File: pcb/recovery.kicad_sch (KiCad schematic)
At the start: 9 parts, among them Q1 SiS454DN

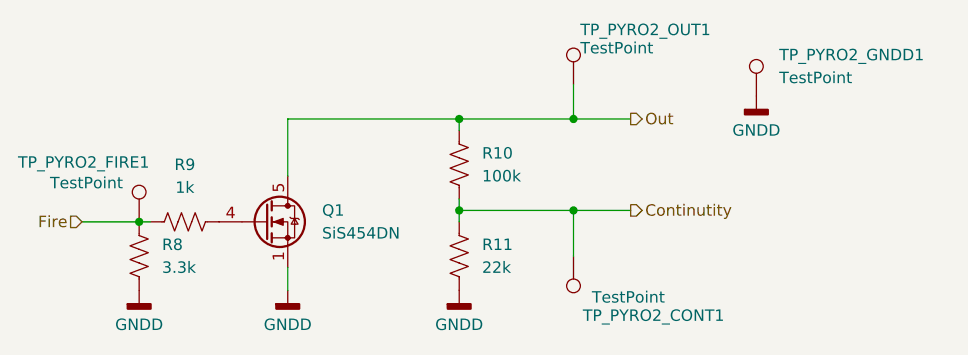
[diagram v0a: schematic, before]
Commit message: Updated schematics and removed most test points
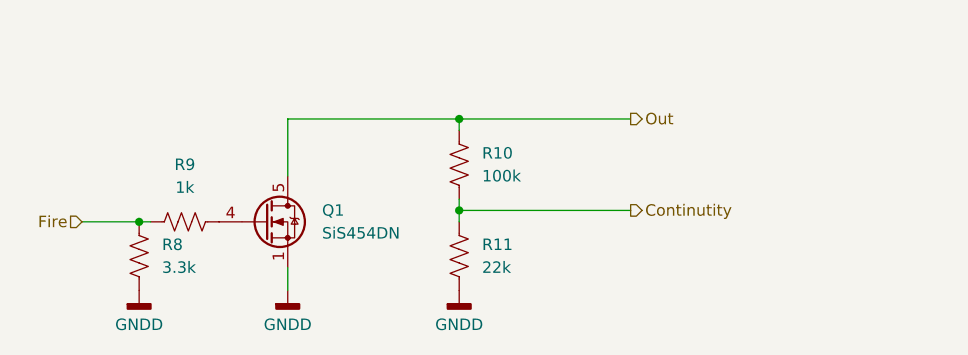
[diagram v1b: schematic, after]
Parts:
- removed TP_PYRO2_CONT1, TP_PYRO2_FIRE1, TP_PYRO2_GNDD1, TP_PYRO2_OUT1: TestPoint, TestPoint:TestPoint_Loop_D2.54mm_Drill1.5mm_Beaded, symbol Connector:TestPoint
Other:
- title: (none) -> Control Module Rev2
